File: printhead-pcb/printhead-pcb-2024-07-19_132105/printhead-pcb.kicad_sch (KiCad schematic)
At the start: 25 parts, among them J1 Power, J3 DATA, U1 PCA9615DP, U6 AP7361C-33E

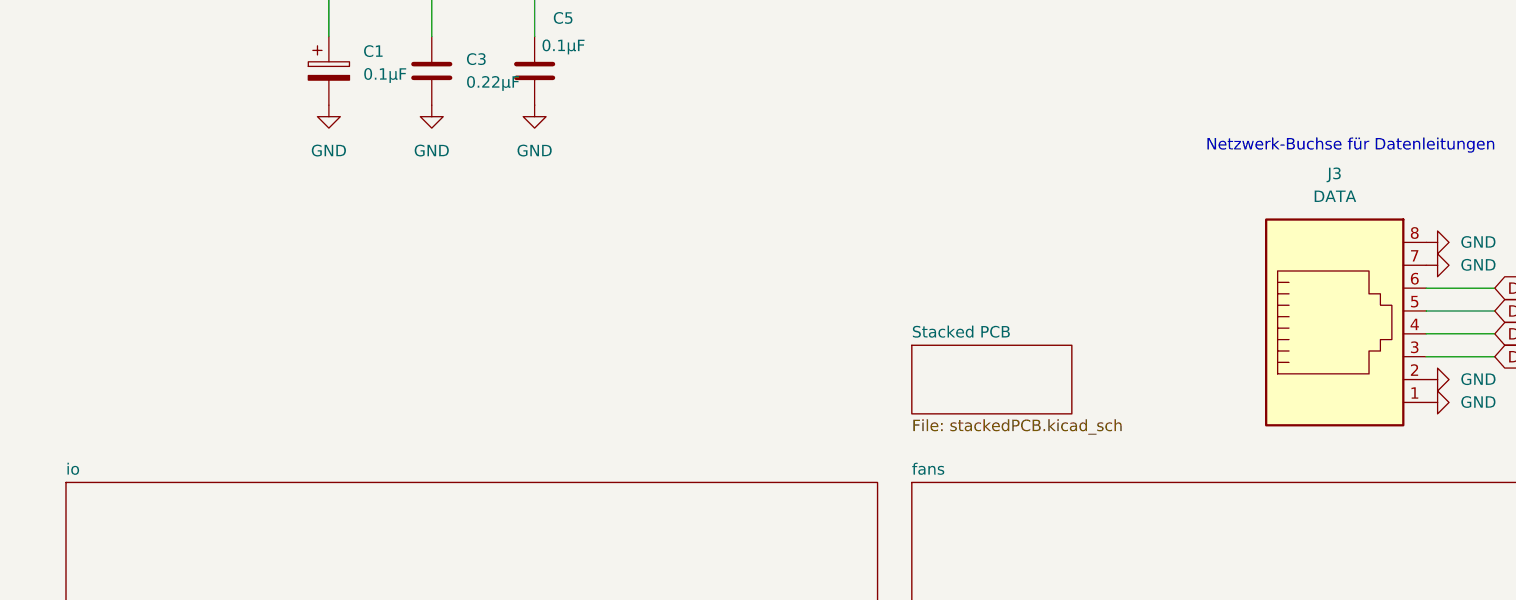
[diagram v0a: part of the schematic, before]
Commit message: made first pcb design of module 1 with components on front and back
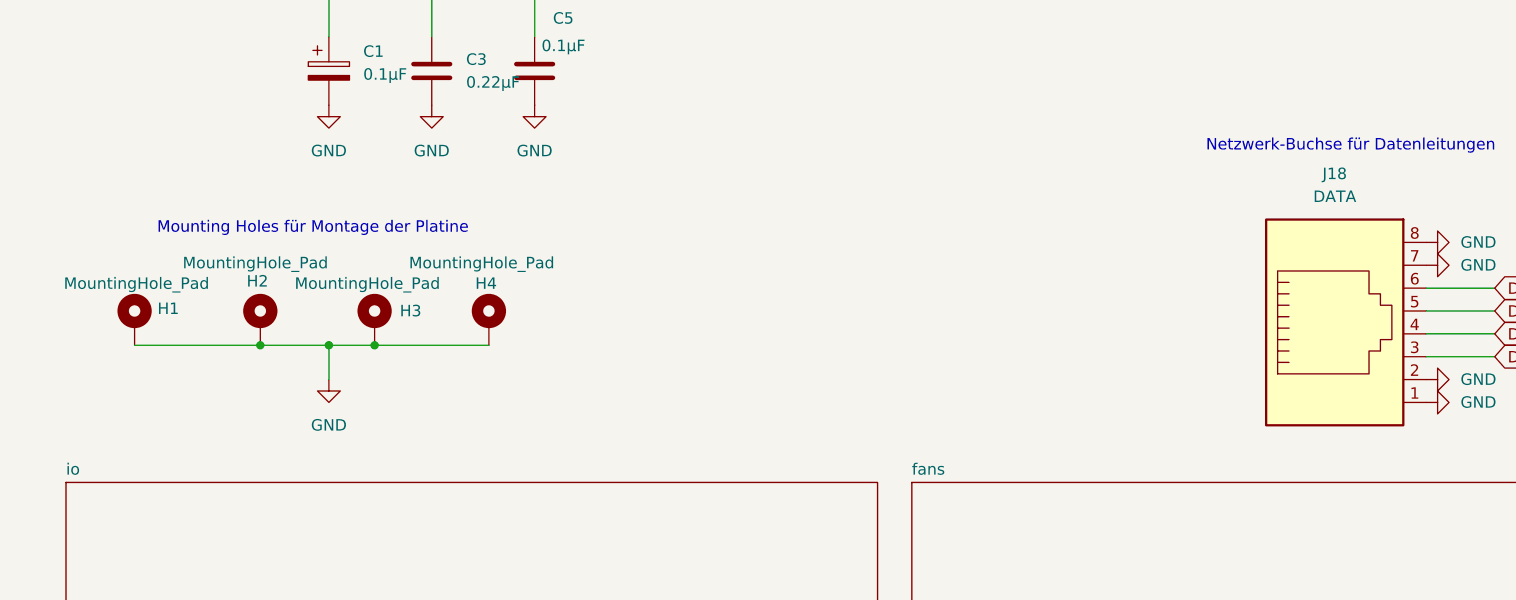
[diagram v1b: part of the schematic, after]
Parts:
- added H1, H2, H3, H4: MountingHole_Pad, MountingHole:MountingHole_2.2mm_M2_Pad_TopBottom, symbol Mechanical:MountingHole_Pad
- J1: footprint Connector_PinHeader_2.54mm:PinHeader_1x03_P2.54mm_Horizontal -> Connector_JST:JST_EH_S3B-EH_1x03_P2.50mm_Horizontal
- renumbered J3 to J18
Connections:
- net GND: now also H1.1, H2.1, H3.1, H4.1
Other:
- removed sheet Stacked PCB
- note added: "Mounting Holes für Montage der Platine"
